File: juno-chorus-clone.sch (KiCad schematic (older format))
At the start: 173 parts

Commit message: schematics fixes
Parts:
- gave numbers to parts that had none: 169
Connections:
- wire segments 585 -> 579
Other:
- moved on the sheet: D7, Q17, R19, R24, U4A

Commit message: missing names
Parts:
- Q11, Q12, Q14, Q15, Q18, Q19: value PNP -> 2SA1015
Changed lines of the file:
@@
 P 13750 1400
 F 0 "Q18" H 13750 1250 60  0000 R CNN
-F 1 "PNP" H 13750 1550 60  0000 R CNN
+F 1 "2SA1015" H 13750 1550 60  0000 R CNN
 F 2 "~" H 13750 1400 60  0000 C CNN
 F 3 "~" H 13750 1400 60  0000 C CNN
@@
 P 15300 1650
 F 0 "Q19" H 15300 1500 60  0000 R CNN
-F 1 "PNP" H 15300 1800 60  0000 R CNN
+F 1 "2SA1015" H 15300 1800 60  0000 R CNN
 F 2 "~" H 15300 1650 60  0000 C CNN
 F 3 "~" H 15300 1650 60  0000 C CNN
@@
 P 10050 3100
 F 0 "Q11" H 10050 2950 60  0000 R CNN
-F 1 "PNP" H 10050 3250 60  0000 R CNN
+F 1 "2SA1015" H 10050 3250 60  0000 R CNN
 F 2 "~" H 10050 3100 60  0000 C CNN
 F 3 "~" H 10050 3100 60  0000 C CNN
@@
 P 11600 3350
 F 0 "Q14" H 11600 3200 60  0000 R CNN
-F 1 "PNP" H 11600 3500 60  0000 R CNN
+F 1 "2SA1015" H 11600 3500 60  0000 R CNN
 F 2 "~" H 11600 3350 60  0000 C CNN
 F 3 "~" H 11600 3350 60  0000 C CNN
@@
 P 10050 6250
 F 0 "Q12" H 10050 6100 60  0000 R CNN
-F 1 "PNP" H 10050 6400 60  0000 R CNN
+F 1 "2SA1015" H 10050 6400 60  0000 R CNN
 F 2 "~" H 10050 6250 60  0000 C CNN
 F 3 "~" H 10050 6250 60  0000 C CNN
@@
 P 11600 6500
 F 0 "Q15" H 11600 6350 60  0000 R CNN
-F 1 "PNP" H 11600 6650 60  0000 R CNN
+F 1 "2SA1015" H 11600 6650 60  0000 R CNN
 F 2 "~" H 11600 6500 60  0000 C CNN
 F 3 "~" H 11600 6500 60  0000 C CNN

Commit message: fix transistors pinouts
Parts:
- removed Q1, Q10, Q13, Q2, Q5, Q6, Q9: 2SC1815, ~, symbol NPN
- removed Q11, Q12, Q14, Q15, Q18, Q19, Q3, Q4, Q7, Q8: 2SA1015, ~, symbol PNP
- added Q? (x7): 2SC1815, TO92, symbol 2SC1815
- added Q? (x10): 2SA1015, TO92, symbol 2SA1016
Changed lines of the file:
@@
 $EndComp
 $Comp
-L PNP Q18
-U 1 1 53551E04
-P 13750 1400
-F 0 "Q18" H 13750 1250 60  0000 R CNN
-F 1 "2SA1015" H 13750 1550 60  0000 R CNN
-F 2 "~" H 13750 1400 60  0000 C CNN
-F 3 "~" H 13750 1400 60  0000 C CNN
-	1    13750 1400
-	1    0    0    -1
-$EndComp
-$Comp
-L PNP Q19
-U 1 1 53551E11
-P 15300 1650
-F 0 "Q19" H 15300 1500 60  0000 R CNN
-F 1 "2SA1015" H 15300 1800 60  0000 R CNN
-F 2 "~" H 15300 1650 60  0000 C CNN
-F 3 "~" H 15300 1650 60  0000 C CNN
-	1    15300 1650
-	1    0    0    -1
-$EndComp
-$Comp
 L R R75
 U 1 1 53551E17
@@
 $EndComp
 $Comp
-L PNP Q11
-U 1 1 535534CB
-P 10050 3100
-F 0 "Q11" H 10050 2950 60  0000 R CNN
-F 1 "2SA1015" H 10050 3250 60  0000 R CNN
-F 2 "~" H 10050 3100 60  0000 C CNN
-F 3 "~" H 10050 3100 60  0000 C CNN
-	1    10050 3100
-	1    0    0    -1
-$EndComp
-$Comp
-L PNP Q14
-U 1 1 535534D1
-P 11600 3350
-F 0 "Q14" H 11600 3200 60  0000 R CNN
-F 1 "2SA1015" H 11600 3500 60  0000 R CNN
-F 2 "~" H 11600 3350 60  0000 C CNN
-F 3 "~" H 11600 3350 60  0000 C CNN
-	1    11600 3350
-	1    0    0    -1
-$EndComp
-$Comp
 L R R51
 U 1 1 535534D7
@@
 $EndComp
 $Comp
-L PNP Q3
-U 1 1 53556CA1
-P 3100 3650
-F 0 "Q3" H 3100 3500 60  0000 R CNN
-F 1 "2SA1015" H 3100 3800 60  0000 R CNN
-F 2 "~" H 3100 3650 60  0000 C CNN
-F 3 "~" H 3100 3650 60  0000 C CNN
-	1    3100 3650
-	1    0    0    1
-$EndComp
-$Comp
-L PNP Q7
-U 1 1 53556CA7
-P 3900 3650
-F 0 "Q7" H 3900 3500 60  0000 R CNN
-F 1 "2SA1015" H 3900 3800 60  0000 R CNN
-F 2 "~" H 3900 3650 60  0000 C CNN
-F 3 "~" H 3900 3650 60  0000 C CNN
-	1    3900 3650
-	-1   0    0    1
-$EndComp
-$Comp
 L R R16
 U 1 1 53556CCB
@@
 $EndComp
 $Comp
-L NPN Q1
-U 1 1 53557C7A
-P 2800 4250
-F 0 "Q1" H 2800 4100 50  0000 R CNN
-F 1 "2SC1815" H 2800 4400 50  0000 R CNN
-F 2 "~" H 2800 4250 60  0000 C CNN
-F 3 "~" H 2800 4250 60  0000 C CNN
-	1    2800 4250
-	-1   0    0    -1
-$EndComp
-$Comp
-L NPN Q9
-U 1 1 53557C87
-P 4750 4500
-F 0 "Q9" H 4750 4350 50  0000 R CNN
-F 1 "2SC1815" H 4750 4650 50  0000 R CNN
-F 2 "~" H 4750 4500 60  0000 C CNN
-F 3 "~" H 4750 4500 60  0000 C CNN
-	1    4750 4500
-	-1   0    0    -1
-$EndComp
-$Comp
-L NPN Q5
-U 1 1 53557C8D
-P 3700 4500
-F 0 "Q5" H 3700 4350 50  0000 R CNN
-F 1 "2SC1815" H 4150 4250 50  0000 R CNN
-F 2 "~" H 3700 4500 60  0000 C CNN
-F 3 "~" H 3700 4500 60  0000 C CNN
-	1    3700 4500
-	1    0    0    -1
-$EndComp
-$Comp
 L DIODE D3
 U 1 1 53557CA9
 P 3450 4250
-F 0 "D3" H 3450 4350 40  0000 C CNN
+F 0 "D3" H 3450 4100 40  0000 C CNN
 F 1 "1N4148" H 3450 4150 40  0000 C CNN
 F 2 "~" H 3450 4250 60  0000 C CNN
@@
 $EndComp
 $Comp
-L PNP Q12
-U 1 1 5355E89A
-P 10050 6250
-F 0 "Q12" H 10050 6100 60  0000 R CNN
-F 1 "2SA1015" H 10050 6400 60  0000 R CNN
-F 2 "~" H 10050 6250 60  0000 C CNN
-F 3 "~" H 10050 6250 60  0000 C CNN
-	1    10050 6250
-	1    0    0    -1
-$EndComp
-$Comp
-L PNP Q15
-U 1 1 5355E8A0
-P 11600 6500
-F 0 "Q15" H 11600 6350 60  0000 R CNN
-F 1 "2SA1015" H 11600 6650 60  0000 R CNN
-F 2 "~" H 11600 6500 60  0000 C CNN
-F 3 "~" H 11600 6500 60  0000 C CNN
-	1    11600 6500
-	1    0    0    -1
-$EndComp
-$Comp
 L R R53
 U 1 1 5355E8A6
@@
 $EndComp
 $Comp
-L PNP Q4
-U 1 1 5355E9D7
-P 3100 6800
-F 0 "Q4" H 3100 6650 60  0000 R CNN
-F 1 "2SA1015" H 3100 6950 60  0000 R CNN
-F 2 "~" H 3100 6800 60  0000 C CNN
-F 3 "~" H 3100 6800 60  0000 C CNN
-	1    3100 6800
-	1    0    0    1
-$EndComp
-$Comp
-L PNP Q8
-U 1 1 5355E9DD
-P 3900 6800
-F 0 "Q8" H 3900 6650 60  0000 R CNN
-F 1 "2SA1015" H 3900 6950 60  0000 R CNN
-F 2 "~" H 3900 6800 60  0000 C CNN
-F 3 "~" H 3900 6800 60  0000 C CNN
-	1    3900 6800
-	-1   0    0    1
-$EndComp
-$Comp
 L R R18
 U 1 1 5355E9E3
@@
 $EndComp
 $Comp
-L NPN Q2
-U 1 1 5355EA1C
-P 2800 7400
-F 0 "Q2" H 2800 7250 50  0000 R CNN
-F 1 "2SC1815" H 2800 7550 50  0000 R CNN
-F 2 "~" H 2800 7400 60  0000 C CNN
-F 3 "~" H 2800 7400 60  0000 C CNN
-	1    2800 7400
-	-1   0    0    -1
-$EndComp
-$Comp
-L NPN Q10
-U 1 1 5355EA22
-P 4750 7650
-F 0 "Q10" H 4750 7500 50  0000 R CNN
-F 1 "2SC1815" H 4750 7800 50  0000 R CNN
-F 2 "~" H 4750 7650 60  0000 C CNN
-F 3 "~" H 4750 7650 60  0000 C CNN
-	1    4750 7650
-	-1   0    0    -1
-$EndComp
-$Comp
-L NPN Q6
-U 1 1 5355EA28
-P 3700 7650
-F 0 "Q6" H 3700 7500 50  0000 R CNN
-F 1 "2SC1815" H 4150 7400 50  0000 R CNN
-F 2 "~" H 3700 7650 60  0000 C CNN
-F 3 "~" H 3700 7650 60  0000 C CNN
-	1    3700 7650
-	1    0    0    -1
-$EndComp
-$Comp
 L DIODE D4
 U 1 1 5355EA2E
 P 3450 7400
-F 0 "D4" H 3450 7500 40  0000 C CNN
+F 0 "D4" H 3450 7250 40  0000 C CNN
 F 1 "1N4148" H 3450 7300 40  0000 C CNN
 F 2 "~" H 3450 7400 60  0000 C CNN
@@
 $EndComp
 $Comp
-L NPN Q13
-U 1 1 53562560
-P 10600 4700
-F 0 "Q13" H 10600 4550 50  0000 R CNN
-F 1 "2SC1815" H 11050 4450 50  0000 R CNN
-F 2 "~" H 10600 4700 60  0000 C CNN
-F 3 "~" H 10600 4700 60  0000 C CNN
-	1    10600 4700
-	1    0    0    -1
-$EndComp
-$Comp
 L VAA #PWR41
 U 1 1 53562566
@@
 Connection ~ 6200 4650
 Connection ~ 6200 7800
+$Comp
+L 2SC1815 Q?
+U 1 1 53552843
+P 10600 4700
+F 0 "Q?" H 10600 4551 40  0000 R CNN
+F 1 "2SC1815" H 10600 4850 40  0000 R CNN
+F 2 "TO92" H 10500 4802 29  0000 C CNN
+F 3 "~" H 10600 4700 60  0000 C CNN
+	1    10600 4700
+	1    0    0    -1
+$EndComp
+$Comp
+L 2SC1815 Q?
+U 1 1 5355285A
+P 2800 7400
+F 0 "Q?" H 2800 7251 40  0000 R CNN
+F 1 "2SC1815" H 2800 7550 40  0000 R CNN
+F 2 "TO92" H 2700 7502 29  0000 C CNN
+F 3 "~" H 2800 7400 60  0000 C CNN
+	1    2800 7400
+	-1   0    0    -1
+$EndComp
+$Comp
+L 2SC1815 Q?
+U 1 1 53552860
+P 3700 4500
+F 0 "Q?" H 3700 4351 40  0000 R CNN
+F 1 "2SC1815" H 3700 4650 40  0000 R CNN
+F 2 "TO92" H 3600 4602 29  0000 C CNN
+F 3 "~" H 3700 4500 60  0000 C CNN
+	1    3700 4500
+	1    0    0    -1
+$EndComp
+$Comp
+L 2SC1815 Q?
+U 1 1 53552866
+P 3700 7650
+F 0 "Q?" H 3700 7501 40  0000 R CNN
+F 1 "2SC1815" H 3700 7800 40  0000 R CNN
+F 2 "TO92" H 3600 7752 29  0000 C CNN
+F 3 "~" H 3700 7650 60  0000 C CNN
+	1    3700 7650
+	1    0    0    -1
+$EndComp
+$Comp
+L 2SC1815 Q?
+U 1 1 5355286C
+P 4750 4500
+F 0 "Q?" H 4750 4351 40  0000 R CNN
+F 1 "2SC1815" H 4750 4650 40  0000 R CNN
+F 2 "TO92" H 4650 4602 29  0000 C CNN
+F 3 "~" H 4750 4500 60  0000 C CNN
+	1    4750 4500
+	-1   0    0    -1
+$EndComp
+$Comp
+L 2SC1815 Q?
+U 1 1 53552872
+P 4750 7650
+F 0 "Q?" H 4750 7501 40  0000 R CNN
+F 1 "2SC1815" H 4750 7800 40  0000 R CNN
+F 2 "TO92" H 4650 7752 29  0000 C CNN
+F 3 "~" H 4750 7650 60  0000 C CNN
+	1    4750 7650
+	-1   0    0    -1
+$EndComp
+$Comp
+L 2SC1815 Q?
+U 1 1 53552882
+P 2800 4250
+F 0 "Q?" H 2800 4101 40  0000 R CNN
+F 1 "2SC1815" H 2800 4400 40  0000 R CNN
+F 2 "TO92" H 2700 4352 29  0000 C CNN
+F 3 "~" H 2800 4250 60  0000 C CNN
+	1    2800 4250
+	-1   0    0    -1
+$EndComp
+$Comp
+L 2SA1016 Q?
+U 1 1 5355288A
+P 3900 3650
+F 0 "Q?" H 3900 3501 40  0000 R CNN
+F 1 "2SA1015" H 3900 3800 40  0000 R CNN
+F 2 "TO92" H 3800 3752 29  0000 C CNN
+F 3 "~" H 3900 3650 60  0000 C CNN
+	1    3900 3650
+	-1   0    0    1
+$EndComp
+$Comp
+L 2SA1016 Q?
+U 1 1 535528A6
+P 13750 1400
+F 0 "Q?" H 13750 1251 40  0000 R CNN
+F 1 "2SA1015" H 13750 1550 40  0000 R CNN
+F 2 "TO92" H 13650 1502 29  0000 C CNN
+F 3 "~" H 13750 1400 60  0000 C CNN
+	1    13750 1400
+	1    0    0    -1
+$EndComp
+$Comp
+L 2SA1016 Q?
+U 1 1 535528AC
+P 15300 1650
+F 0 "Q?" H 15300 1501 40  0000 R CNN
+F 1 "2SA1015" H 15300 1800 40  0000 R CNN
+F 2 "TO92" H 15200 1752 29  0000 C CNN
+F 3 "~" H 15300 1650 60  0000 C CNN
+	1    15300 1650
+	1    0    0    -1
+$EndComp
+$Comp
+L 2SA1016 Q?
+U 1 1 535528BC
+P 11600 3350
+F 0 "Q?" H 11600 3201 40  0000 R CNN
+F 1 "2SA1015" H 11600 3500 40  0000 R CNN
+F 2 "TO92" H 11500 3452 29  0000 C CNN
+F 3 "~" H 11600 3350 60  0000 C CNN
+	1    11600 3350
+	1    0    0    -1
+$EndComp
+$Comp
+L 2SA1016 Q?
+U 1 1 535528C2
+P 10050 3100
+F 0 "Q?" H 10050 2951 40  0000 R CNN
+F 1 "2SA1015" H 10050 3250 40  0000 R CNN
+F 2 "TO92" H 9950 3202 29  0000 C CNN
+F 3 "~" H 10050 3100 60  0000 C CNN
+	1    10050 3100
+	1    0    0    -1
+$EndComp
+$Comp
+L 2SA1016 Q?
+U 1 1 535528C8
+P 10050 6250
+F 0 "Q?" H 10050 6101 40  0000 R CNN
+F 1 "2SA1015" H 10050 6400 40  0000 R CNN
+F 2 "TO92" H 9950 6352 29  0000 C CNN
+F 3 "~" H 10050 6250 60  0000 C CNN
+	1    10050 6250
+	1    0    0    -1
+$EndComp
+$Comp
+L 2SA1016 Q?
+U 1 1 535528CE
+P 11600 6500
+F 0 "Q?" H 11600 6351 40  0000 R CNN
+F 1 "2SA1015" H 11600 6650 40  0000 R CNN
+F 2 "TO92" H 11500 6602 29  0000 C CNN
+F 3 "~" H 11600 6500 60  0000 C CNN
+	1    11600 6500
+	1    0    0    -1
+$EndComp
+$Comp
+L 2SA1016 Q?
+U 1 1 535528ED
+P 3100 3650
+F 0 "Q?" H 3100 3501 40  0000 R CNN
+F 1 "2SA1015" H 3100 3800 40  0000 R CNN
+F 2 "TO92" H 3000 3752 29  0000 C CNN
+F 3 "~" H 3100 3650 60  0000 C CNN
+	1    3100 3650
+	1    0    0    1
+$EndComp
+$Comp
+L 2SA1016 Q?
+U 1 1 535528F3
+P 3100 6800
+F 0 "Q?" H 3100 6651 40  0000 R CNN
+F 1 "2SA1015" H 3100 6950 40  0000 R CNN
+F 2 "TO92" H 3000 6902 29  0000 C CNN
+F 3 "~" H 3100 6800 60  0000 C CNN
+	1    3100 6800
+	1    0    0    1
+$EndComp
+$Comp
+L 2SA1016 Q?
+U 1 1 53552903
+P 3900 6800
+F 0 "Q?" H 3900 6651 40  0000 R CNN
+F 1 "2SA1015" H 3900 6950 40  0000 R CNN
+F 2 "TO92" H 3800 6902 29  0000 C CNN
+F 3 "~" H 3900 6800 60  0000 C CNN
+	1    3900 6800
+	-1   0    0    1
+$EndComp
 $EndSCHEMATC

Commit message: annotation
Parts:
- gave numbers to parts that had none: 17
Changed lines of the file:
@@
 Connection ~ 6200 7800
 $Comp
-L 2SC1815 Q?
+L 2SC1815 Q13
 U 1 1 53552843
 P 10600 4700
-F 0 "Q?" H 10600 4551 40  0000 R CNN
+F 0 "Q13" H 10600 4551 40  0000 R CNN
 F 1 "2SC1815" H 10600 4850 40  0000 R CNN
 F 2 "TO92" H 10500 4802 29  0000 C CNN
@@
 $EndComp
 $Comp
-L 2SC1815 Q?
+L 2SC1815 Q2
 U 1 1 5355285A
 P 2800 7400
-F 0 "Q?" H 2800 7251 40  0000 R CNN
+F 0 "Q2" H 2800 7251 40  0000 R CNN
 F 1 "2SC1815" H 2800 7550 40  0000 R CNN
 F 2 "TO92" H 2700 7502 29  0000 C CNN
@@
 $EndComp
 $Comp
-L 2SC1815 Q?
+L 2SC1815 Q5
 U 1 1 53552860
 P 3700 4500
-F 0 "Q?" H 3700 4351 40  0000 R CNN
+F 0 "Q5" H 3700 4351 40  0000 R CNN
 F 1 "2SC1815" H 3700 4650 40  0000 R CNN
 F 2 "TO92" H 3600 4602 29  0000 C CNN
@@
 $EndComp
 $Comp
-L 2SC1815 Q?
+L 2SC1815 Q6
 U 1 1 53552866
 P 3700 7650
-F 0 "Q?" H 3700 7501 40  0000 R CNN
+F 0 "Q6" H 3700 7501 40  0000 R CNN
 F 1 "2SC1815" H 3700 7800 40  0000 R CNN
 F 2 "TO92" H 3600 7752 29  0000 C CNN
@@
 $EndComp
 $Comp
-L 2SC1815 Q?
+L 2SC1815 Q9
 U 1 1 5355286C
 P 4750 4500
-F 0 "Q?" H 4750 4351 40  0000 R CNN
+F 0 "Q9" H 4750 4351 40  0000 R CNN
 F 1 "2SC1815" H 4750 4650 40  0000 R CNN
 F 2 "TO92" H 4650 4602 29  0000 C CNN
@@
 $EndComp
 $Comp
-L 2SC1815 Q?
+L 2SC1815 Q10
 U 1 1 53552872
 P 4750 7650
-F 0 "Q?" H 4750 7501 40  0000 R CNN
+F 0 "Q10" H 4750 7501 40  0000 R CNN
 F 1 "2SC1815" H 4750 7800 40  0000 R CNN
 F 2 "TO92" H 4650 7752 29  0000 C CNN
@@
 $EndComp
 $Comp
-L 2SC1815 Q?
+L 2SC1815 Q1
 U 1 1 53552882
 P 2800 4250
-F 0 "Q?" H 2800 4101 40  0000 R CNN
+F 0 "Q1" H 2800 4101 40  0000 R CNN
 F 1 "2SC1815" H 2800 4400 40  0000 R CNN
 F 2 "TO92" H 2700 4352 29  0000 C CNN
@@
 $EndComp
 $Comp
-L 2SA1016 Q?
+L 2SA1016 Q7
 U 1 1 5355288A
 P 3900 3650
-F 0 "Q?" H 3900 3501 40  0000 R CNN
+F 0 "Q7" H 3900 3501 40  0000 R CNN
 F 1 "2SA1015" H 3900 3800 40  0000 R CNN
 F 2 "TO92" H 3800 3752 29  0000 C CNN
@@
 $EndComp
 $Comp
-L 2SA1016 Q?
+L 2SA1016 Q18
 U 1 1 535528A6
 P 13750 1400
-F 0 "Q?" H 13750 1251 40  0000 R CNN
+F 0 "Q18" H 13750 1251 40  0000 R CNN
 F 1 "2SA1015" H 13750 1550 40  0000 R CNN
 F 2 "TO92" H 13650 1502 29  0000 C CNN
@@
 $EndComp
 $Comp
-L 2SA1016 Q?
+L 2SA1016 Q19
 U 1 1 535528AC
 P 15300 1650
-F 0 "Q?" H 15300 1501 40  0000 R CNN
+F 0 "Q19" H 15300 1501 40  0000 R CNN
 F 1 "2SA1015" H 15300 1800 40  0000 R CNN
 F 2 "TO92" H 15200 1752 29  0000 C CNN
@@
 $EndComp
 $Comp
-L 2SA1016 Q?
+L 2SA1016 Q14
 U 1 1 535528BC
 P 11600 3350
-F 0 "Q?" H 11600 3201 40  0000 R CNN
+F 0 "Q14" H 11600 3201 40  0000 R CNN
 F 1 "2SA1015" H 11600 3500 40  0000 R CNN
 F 2 "TO92" H 11500 3452 29  0000 C CNN
@@
 $EndComp
 $Comp
-L 2SA1016 Q?
+L 2SA1016 Q11
 U 1 1 535528C2
 P 10050 3100
-F 0 "Q?" H 10050 2951 40  0000 R CNN
+F 0 "Q11" H 10050 2951 40  0000 R CNN
 F 1 "2SA1015" H 10050 3250 40  0000 R CNN
 F 2 "TO92" H 9950 3202 29  0000 C CNN
@@
 $EndComp
 $Comp
-L 2SA1016 Q?
+L 2SA1016 Q12
 U 1 1 535528C8
 P 10050 6250
-F 0 "Q?" H 10050 6101 40  0000 R CNN
+F 0 "Q12" H 10050 6101 40  0000 R CNN
 F 1 "2SA1015" H 10050 6400 40  0000 R CNN
 F 2 "TO92" H 9950 6352 29  0000 C CNN
@@
 $EndComp
 $Comp
-L 2SA1016 Q?
+L 2SA1016 Q15
 U 1 1 535528CE
 P 11600 6500
-F 0 "Q?" H 11600 6351 40  0000 R CNN
+F 0 "Q15" H 11600 6351 40  0000 R CNN
 F 1 "2SA1015" H 11600 6650 40  0000 R CNN
 F 2 "TO92" H 11500 6602 29  0000 C CNN
@@
 $EndComp
 $Comp
-L 2SA1016 Q?
+L 2SA1016 Q3
 U 1 1 535528ED
 P 3100 3650
-F 0 "Q?" H 3100 3501 40  0000 R CNN
+F 0 "Q3" H 3100 3501 40  0000 R CNN
 F 1 "2SA1015" H 3100 3800 40  0000 R CNN
 F 2 "TO92" H 3000 3752 29  0000 C CNN
@@
 $EndComp
 $Comp
-L 2SA1016 Q?
+L 2SA1016 Q4
 U 1 1 535528F3
 P 3100 6800
-F 0 "Q?" H 3100 6651 40  0000 R CNN
+F 0 "Q4" H 3100 6651 40  0000 R CNN
 F 1 "2SA1015" H 3100 6950 40  0000 R CNN
 F 2 "TO92" H 3000 6902 29  0000 C CNN
@@
 $EndComp
 $Comp
-L 2SA1016 Q?
+L 2SA1016 Q8
 U 1 1 53552903
 P 3900 6800
-F 0 "Q?" H 3900 6651 40  0000 R CNN
+F 0 "Q8" H 3900 6651 40  0000 R CNN
 F 1 "2SA1015" H 3900 6950 40  0000 R CNN
 F 2 "TO92" H 3800 6902 29  0000 C CNN

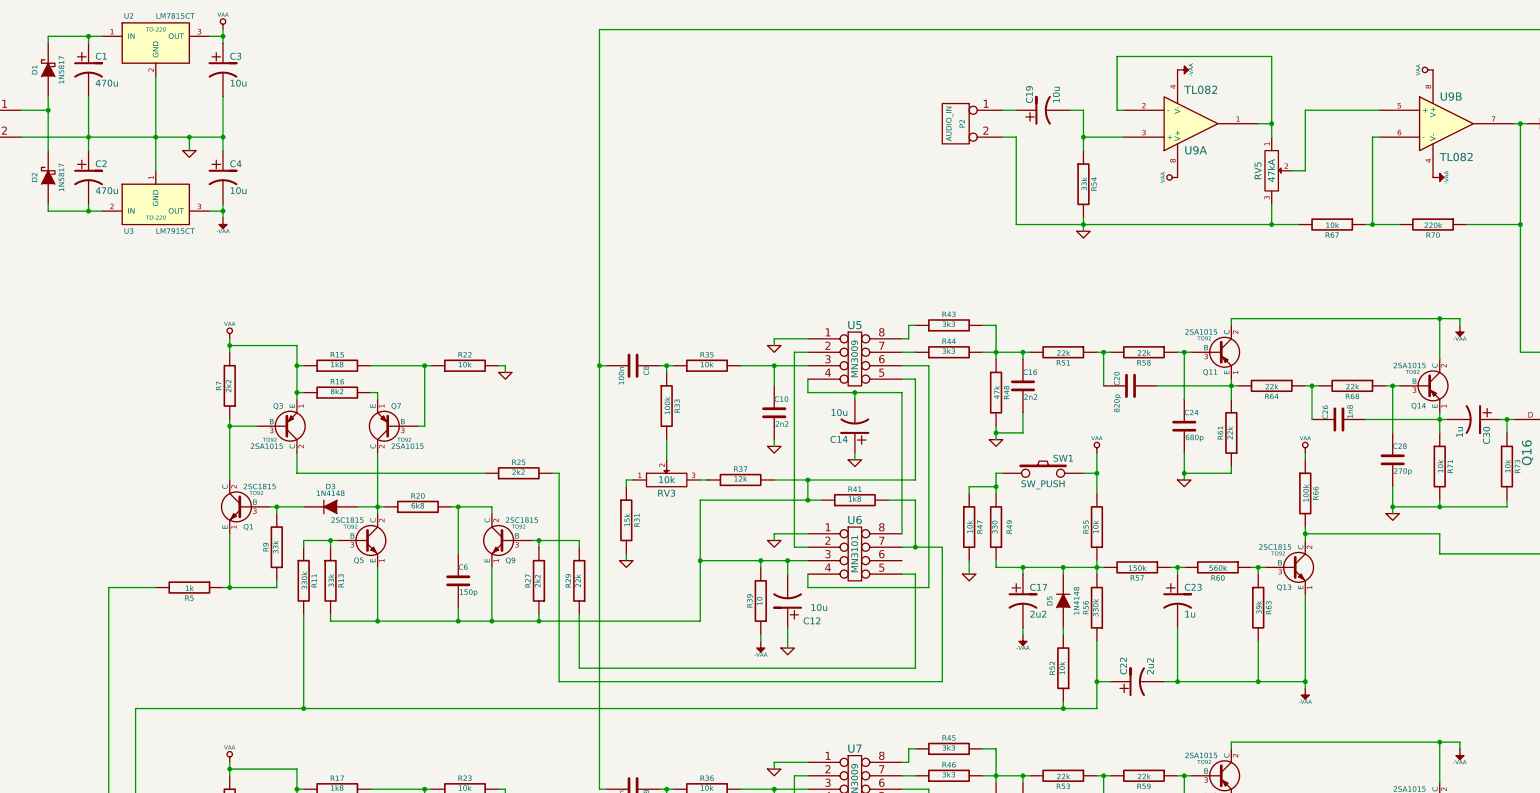
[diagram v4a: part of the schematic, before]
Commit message: schematics: fixes to make it work (tested)
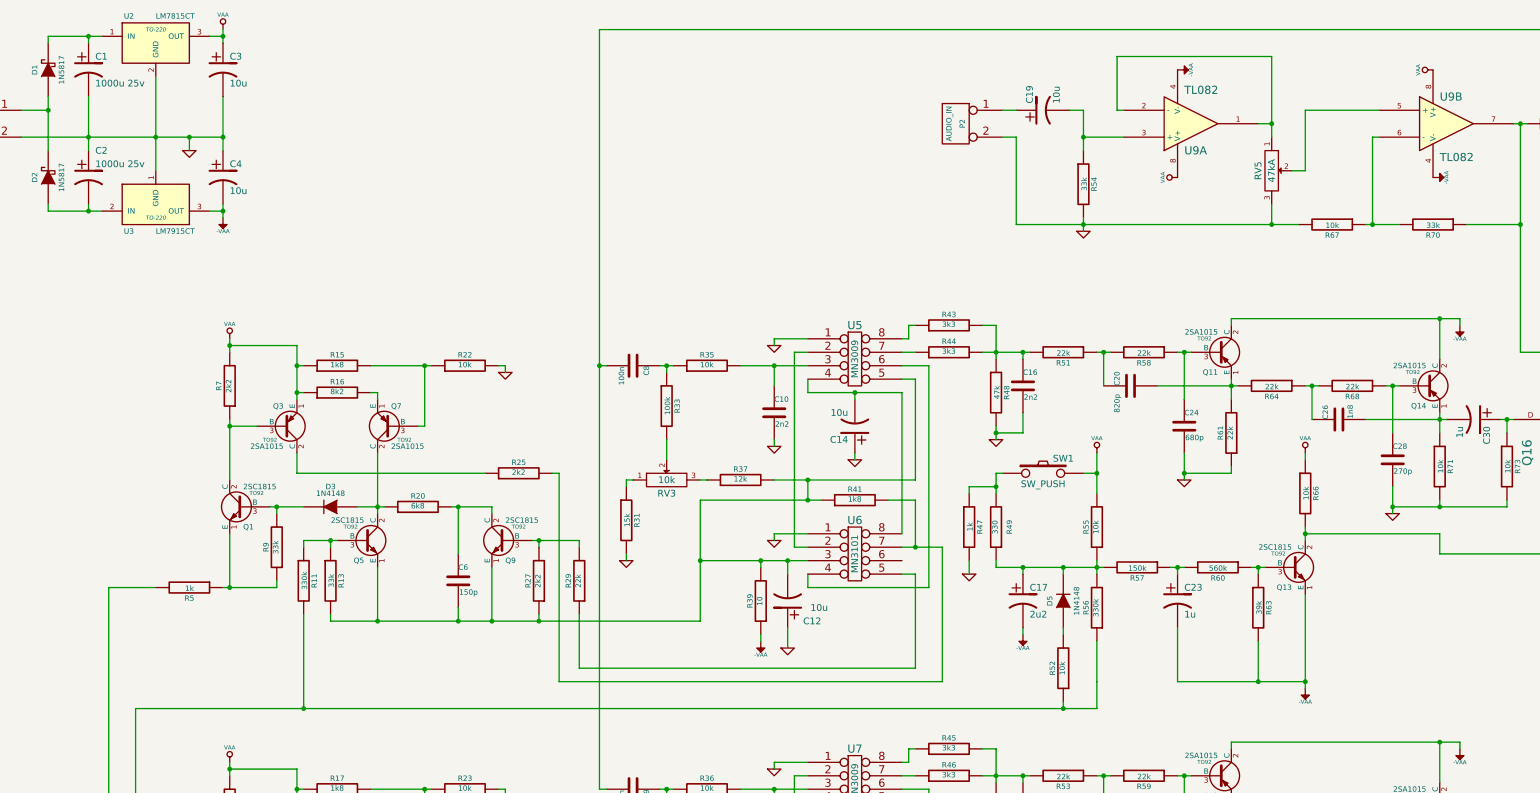
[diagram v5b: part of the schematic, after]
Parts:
- removed C22: 2u2, ~, symbol CP1
- C1, C2: value 470u -> 1000u 25v
- R47: value 10k -> 1k
- R66: value 100k -> 10k
- R70: value 220k -> 33k
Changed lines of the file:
@@
 Sheet 1 1
 Title "Roland Juno-60 chorus board clone"
-Date "21 apr 2014"
-Rev "1"
+Date "3 may 2014"
+Rev "2"
 Comp "GliGli's DIY"
 Comment1 ""
@@
 U 1 1 5354F958
 P 1650 1800
-F 0 "C2" H 1700 1900 50  0000 L CNN
-F 1 "470u" H 1700 1700 50  0000 L CNN
+F 0 "C2" H 1700 2000 50  0000 L CNN
+F 1 "1000u 25v" H 1700 1900 50  0000 L CNN
 F 2 "~" H 1650 1800 60  0000 C CNN
 F 3 "~" H 1650 1800 60  0000 C CNN
@@
 P 1650 1000
 F 0 "C1" H 1700 1100 50  0000 L CNN
-F 1 "470u" H 1700 900 50  0000 L CNN
+F 1 "1000u 25v" H 1700 900 50  0000 L CNN
 F 2 "~" H 1650 1000 60  0000 C CNN
 F 3 "~" H 1650 1000 60  0000 C CNN
@@
 P 11650 2150
 F 0 "R70" V 11730 2150 40  0000 C CNN
-F 1 "220k" V 11657 2151 40  0000 C CNN
+F 1 "33k" V 11657 2151 40  0000 C CNN
 F 2 "~" V 11580 2150 30  0000 C CNN
 F 3 "~" H 11650 2150 30  0000 C CNN
@@
 P 10700 4150
 F 0 "R66" V 10780 4150 40  0000 C CNN
-F 1 "100k" V 10707 4151 40  0000 C CNN
+F 1 "10k" V 10707 4151 40  0000 C CNN
 F 2 "~" V 10630 4150 30  0000 C CNN
 F 3 "~" H 10700 4150 30  0000 C CNN
@@
 $EndComp
 $Comp
-L CP1 C22
-U 1 1 53562B9B
-P 9450 5550
-F 0 "C22" H 9500 5650 50  0000 L CNN
-F 1 "2u2" H 9500 5450 50  0000 L CNN
-F 2 "~" H 9450 5550 60  0000 C CNN
-F 3 "~" H 9450 5550 60  0000 C CNN
-	1    9450 5550
-	0    -1   -1   0
-$EndComp
-$Comp
 L VAA #PWR36
 U 1 1 5356522E
@@
 	10700 3900 10700 3850
 Wire Wire Line
-	9650 5550 9750 5550
-Wire Wire Line
 	9750 5550 10350 5550
 Wire Wire Line
@@
 Wire Wire Line
 	9750 5150 9750 5550
-Connection ~ 9750 5550
 Wire Wire Line
 	8900 5750 8900 5700
@@
 	9150 5550 9150 5250
 Wire Wire Line
-	9250 5550 9150 5550
-Connection ~ 9150 5550
-Wire Wire Line
 	8900 5200 8900 5150
 Wire Wire Line
@@
 P 8200 4400
 F 0 "R47" V 8280 4400 40  0000 C CNN
-F 1 "10k" V 8207 4401 40  0000 C CNN
+F 1 "1k" V 8207 4401 40  0000 C CNN
 F 2 "~" V 8130 4400 30  0000 C CNN
 F 3 "~" H 8200 4400 30  0000 C CNN

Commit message: pcb: v2 with post-debug fixes, should be ok to build
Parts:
- P4: value AUDIO_OUT_1 -> AUDIO_OUT_2
